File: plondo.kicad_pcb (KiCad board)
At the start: 2 copper layers, 243.8 x 114.3 mm, 134 parts, among them J1 AVR ISP, J2 USB4085, SW0 MX_SW_HS, SW1 MX_SW_HS, SW10 MX_SW_HS, SW11 MX_SW_HS, SW12 MX_SW_HS, SW13 MX_SW_HS, SW14 MX_SW_HS, SW15 MX_SW_HS, SW16 MX_SW_HS, SW17 MX_SW_HS, SW18 MX_SW_HS, SW19 MX_SW_HS, SW2 MX_SW_HS, SW20 MX_SW_HS, SW21 MX_SW_HS, SW22 MX_SW_HS, SW23 MX_SW_HS, SW24 MX_SW_HS, SW25 MX_SW_HS, SW26 MX_SW_HS, SW27 MX_SW_HS, SW28 MX_SW_HS, SW29 MX_SW_HS, SW3 MX_SW_HS, SW30 MX_SW_HS, SW31 MX_SW_HS, SW32 MX_SW_HS, SW33 MX_SW_HS, SW34 MX_SW_HS, SW35 MX_SW_HS, SW36 MX_SW_HS, SW37 MX_SW_HS, SW38 MX_SW_HS, SW39 MX_SW_HS, SW4 MX_SW_HS, SW40 MX_SW_HS, SW41 MX_SW_HS, SW42 MX_SW_HS, SW43 MX_SW_HS, SW44 MX_SW_HS, SW45 MX_SW_HS, SW46 MX_SW_HS, SW47 MX_SW_HS, SW5 MX_SW_HS, SW6 MX_SW_HS, SW7 MX_SW_HS, SW8 MX_SW_HS, SW9 MX_SW_HS, U1 ATmega32A-P, Y1 16MHz

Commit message: add ground planes, make vcc lines thicker
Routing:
- net GND: track 339.6 -> 341.0 mm
- net Net-(F1-Pad1): track 16.6 -> 17.9 mm
- added copper zone on B.Cu, net GND
- added copper zone on F.Cu, net GND
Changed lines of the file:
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@@
   (segment (start 176.53 36.576) (end 175.169 35.215) (width 0.25) (layer "B.Cu") (net 1))
   (segment (start 175.169 35.215) (end 163.905 35.215) (width 0.25) (layer "B.Cu") (net 1))
-  (segment (start 240.865 35.210381) (end 239.690619 34.036) (width 0.25) (layer "F.Cu") (net 2))
-  (segment (start 241.808 34.544) (end 240.865 35.487) (width 0.25) (layer "F.Cu") (net 2))
+  (segment (start 241.046 34.29) (end 227.965 34.29) (width 0.25) (layer "F.Cu") (net 2))
   (segment (start 226.695 33.02) (end 223.52 33.02) (width 0.25) (layer "F.Cu") (net 2))
   (segment (start 206.061443 34.563557) (end 200.66 39.965) (width 0.25) (layer "F.Cu") (net 2))
   (segment (start 211.47 36.2) (end 209.833557 34.563557) (width 0.25) (layer "F.Cu") (net 2))
-  (segment (start 246.126 34.544) (end 241.808 34.544) (width 0.25) (layer "F.Cu") (net 2))
+  (segment (start 245.872 33.528) (end 241.808 33.528) (width 0.25) (layer "F.Cu") (net 2))
   (segment (start 241.935 59.055) (end 223.647 59.055) (width 0.25) (layer "F.Cu") (net 2))
+  (segment (start 240.865 35.67) (end 240.865 34.471) (width 0.25) (layer "F.Cu") (net 2))
   (segment (start 145.975 39.715) (end 163.905 39.715) (width 0.25) (layer "F.Cu") (net 2))
+  (segment (start 240.865 34.471) (end 241.173 34.163) (width 0.25) (layer "F.Cu") (net 2))
   (segment (start 196.215 34.965) (end 191.77 39.41) (width 0.25) (layer "F.Cu") (net 2))
   (segment (start 191.77 39.41) (end 191.77 43.18) (width 0.25) (layer "F.Cu") (net 2))
   (segment (start 240.865 35.67) (end 240.865 37.02) (width 0.25) (layer "F.Cu") (net 2))
   (segment (start 246.815 35.67) (end 246.815 37.02) (width 0.25) (layer "F.Cu") (net 2))
-  (segment (start 239.690619 34.036) (end 227.711 34.036) (width 0.25) (layer "F.Cu") (net 2))
   (segment (start 254.37 53.34) (end 248.655 59.055) (width 0.25) (layer "F.Cu") (net 2))
   (segment (start 216.39637 61.595) (end 195.54 61.595) (width 0.25) (layer "F.Cu") (net 2))
   (segment (start 223.647 59.055) (end 221.234 56.642) (width 0.25) (layer "F.Cu") (net 2))
-  (segment (start 246.815 35.67) (end 246.815 35.233) (width 0.25) (layer "F.Cu") (net 2))
-  (segment (start 240.865 35.487) (end 240.865 35.67) (width 0.25) (layer "F.Cu") (net 2))
   (segment (start 195.54 59.65) (end 194.31 58.42) (width 0.25) (layer "F.Cu") (net 2))
   (segment (start 248.655 59.055) (end 245.745 59.055) (width 0.25) (layer "F.Cu") (net 2))
+  (segment (start 246.815 34.471) (end 245.872 33.528) (width 0.25) (layer "F.Cu") (net 2))
   (segment (start 200.66 39.41) (end 200.66 39.965) (width 0.25) (layer "F.Cu") (net 2))
   (segment (start 220.98 55.88) (end 220.98 57.01137) (width 0.25) (layer "F.Cu") (net 2))
@@
   (segment (start 239.014 43.942) (end 236.474 43.942) (width 0.25) (layer "F.Cu") (net 2))
   (segment (start 236.474 43.942) (end 234.95 45.466) (width 0.25) (layer "F.Cu") (net 2))
-  (segment (start 240.865 35.67) (end 240.865 35.210381) (width 0.25) (layer "F.Cu") (net 2))
-  (segment (start 246.815 35.233) (end 246.126 34.544) (width 0.25) (layer "F.Cu") (net 2))
+  (segment (start 241.173 34.163) (end 241.046 34.29) (width 0.25) (layer "F.Cu") (net 2))
   (segment (start 234.95 45.466) (end 234.95 47.395) (width 0.25) (layer "F.Cu") (net 2))
-  (segment (start 227.711 34.036) (end 226.695 33.02) (width 0.25) (layer "F.Cu") (net 2))
+  (segment (start 227.965 34.29) (end 226.695 33.02) (width 0.25) (layer "F.Cu") (net 2))
+  (segment (start 241.808 33.528) (end 241.173 34.163) (width 0.25) (layer "F.Cu") (net 2))
+  (segment (start 246.815 35.67) (end 246.815 34.471) (width 0.25) (layer "F.Cu") (net 2))
   (segment (start 220.98 57.01137) (end 216.39637 61.595) (width 0.25) (layer "F.Cu") (net 2))
   (segment (start 209.833557 34.563557) (end 206.061443 34.563557) (width 0.25) (layer "F.Cu") (net 2))
@@
   (segment (start 163.449 46.355) (end 165.1 46.355) (width 0.25) (layer "F.Cu") (net 3))
   (segment (start 143.774753 44.996649) (end 144.321402 44.45) (width 0.25) (layer "F.Cu") (net 3))
-  (segment (start 222.631 54.356) (end 230.886 54.356) (width 0.25) (layer "F.Cu") (net 3))
+  (segment (start 222.631 54.356) (end 230.886 54.356) (width 0.5) (layer "F.Cu") (net 3))
   (segment (start 144.321402 44.45) (end 161.544 44.45) (width 0.25) (layer "F.Cu") (net 3))
-  (segment (start 230.886 54.356) (end 231.775 55.245) (width 0.25) (layer "F.Cu") (net 3))
-  (segment (start 197.485 52.705) (end 194.31 49.53) (width 0.25) (layer "F.Cu") (net 3))
+  (segment (start 230.886 54.356) (end 231.775 55.245) (width 0.5) (layer "F.Cu") (net 3))
+  (segment (start 197.485 52.705) (end 194.31 49.53) (width 0.5) (layer "F.Cu") (net 3))
   (segment (start 59.69 42.418) (end 61.468 44.196) (width 0.25) (layer "F.Cu") (net 3))
-  (segment (start 220.98 52.705) (end 197.485 52.705) (width 0.25) (layer "F.Cu") (net 3))
-  (segment (start 197.485 52.705) (end 191.77 58.42) (width 0.25) (layer "F.Cu") (net 3))
+  (segment (start 220.98 52.705) (end 197.485 52.705) (width 0.5) (layer "F.Cu") (net 3))
+  (segment (start 197.485 52.705) (end 191.77 58.42) (width 0.5) (layer "F.Cu") (net 3))
   (segment (start 198.969 34.965) (end 194.31 39.624) (width 0.25) (layer "F.Cu") (net 3))
   (segment (start 194.31 39.624) (end 194.31 43.18) (width 0.25) (layer "F.Cu") (net 3))
-  (segment (start 220.98 52.705) (end 222.631 54.356) (width 0.25) (layer "F.Cu") (net 3))
-  (segment (start 231.775 55.245) (end 233.68 55.245) (width 0.25) (layer "F.Cu") (net 3))
+  (segment (start 220.98 52.705) (end 222.631 54.356) (width 0.5) (layer "F.Cu") (net 3))
+  (segment (start 231.775 55.245) (end 233.68 55.245) (width 0.5) (layer "F.Cu") (net 3))
   (segment (start 190.54 61.595) (end 190.54 59.65) (width 0.25) (layer "F.Cu") (net 3))
-  (segment (start 194.31 49.53) (end 194.31 43.18) (width 0.25) (layer "F.Cu") (net 3))
-  (segment (start 234.95 48.895) (end 238.115 48.895) (width 0.25) (layer "F.Cu") (net 3))
-  (segment (start 238.115 48.895) (end 241.3 45.71) (width 0.25) (layer "F.Cu") (net 3))
+  (segment (start 194.31 49.53) (end 194.31 43.18) (width 0.5) (layer "F.Cu") (net 3))
+  (segment (start 234.95 48.895) (end 238.115 48.895) (width 0.5) (layer "F.Cu") (net 3))
+  (segment (start 238.115 48.895) (end 241.3 45.71) (width 0.5) (layer "F.Cu") (net 3))
   (segment (start 161.544 44.45) (end 163.449 46.355) (width 0.25) (layer "F.Cu") (net 3))
-  (segment (start 234.95 53.975) (end 233.68 55.245) (width 0.25) (layer "F.Cu") (net 3))
+  (segment (start 234.95 53.975) (end 233.68 55.245) (width 0.5) (layer "F.Cu") (net 3))
   (segment (start 59.69 41.021) (end 59.69 42.418) (width 0.25) (layer "F.Cu") (net 3))
   (segment (start 165.1 46.355) (end 179.705 46.355) (width 0.25) (layer "F.Cu") (net 3))
   (segment (start 190.54 59.65) (end 191.77 58.42) (width 0.25) (layer "F.Cu") (net 3))
-  (segment (start 234.95 48.895) (end 234.95 53.975) (width 0.25) (layer "F.Cu") (net 3))
+  (segment (start 234.95 48.895) (end 234.95 53.975) (width 0.5) (layer "F.Cu") (net 3))
   (segment (start 179.705 46.355) (end 191.77 58.42) (width 0.25) (layer "F.Cu") (net 3))
   (via (at 143.774753 44.996649) (size 0.8) (drill 0.4) (layers "F.Cu" "B.Cu") (net 3))
@@
   (segment (start 226.695 47.63) (end 228.6 49.535) (width 0.25) (layer "B.Cu") (net 94))
   (segment (start 243.586 36.322) (end 243.415 36.493) (width 0.25) (layer "B.Cu") (net 94))
-  (segment (start 245.56 34.994) (end 245.965 35.399) (width 0.25) (layer "F.Cu") (net 95))
-  (segment (start 245.965 37.02) (end 245.965 38.701) (width 0.25) (layer "F.Cu") (net 95))
-  (segment (start 245.965 35.67) (end 245.965 37.02) (width 0.25) (layer "F.Cu") (net 95))
-  (segment (start 245.965 35.399) (end 245.965 35.67) (width 0.25) (layer "F.Cu") (net 95))
-  (segment (start 242.321761 34.994) (end 245.56 34.994) (width 0.25) (layer "F.Cu") (net 95))
-  (segment (start 245.965 38.701) (end 246.38 39.116) (width 0.25) (layer "F.Cu") (net 95))
-  (segment (start 241.715 35.600761) (end 242.321761 34.994) (width 0.25) (layer "F.Cu") (net 95))
-  (segment (start 246.38 39.116) (end 246.38 45.72) (width 0.25) (layer "F.Cu") (net 95))
+  (segment (start 242.316 34.29) (end 241.715 34.891) (width 0.5) (layer "F.Cu") (net 95))
+  (segment (start 245.965 35.67) (end 245.965 34.891) (width 0.5) (layer "F.Cu") (net 95))
+  (segment (start 245.965 37.02) (end 245.965 38.701) (width 0.5) (layer "F.Cu") (net 95))
+  (segment (start 245.965 35.67) (end 245.965 37.02) (width 0.5) (layer "F.Cu") (net 95))
+  (segment (start 241.715 34.891) (end 241.715 35.67) (width 0.5) (layer "F.Cu") (net 95))
+  (segment (start 245.965 34.891) (end 245.364 34.29) (width 0.5) (layer "F.Cu") (net 95))
+  (segment (start 245.965 38.701) (end 246.38 39.116) (width 0.5) (layer "F.Cu") (net 95))
+  (segment (start 246.38 39.116) (end 246.38 45.72) (width 0.5) (layer "F.Cu") (net 95))
+  (segment (start 245.364 34.29) (end 242.316 34.29) (width 0.5) (layer "F.Cu") (net 95))
   (segment (start 241.715 35.67) (end 241.715 35.600761) (width 0.25) (layer "F.Cu") (net 95))
-  (segment (start 241.715 35.67) (end 241.715 37.02) (width 0.25) (layer "F.Cu") (net 95))
+  (segment (start 241.715 35.67) (end 241.715 37.02) (width 0.5) (layer "F.Cu") (net 95))
+  (zone (net 2) (net_name "GND") (layer "F.Cu") (hatch edge 0.508)
+    (connect_pads (clearance 0.508))
+    (min_thickness 0.254) (filled_areas_thickness no)
+    (fill yes (thermal_gap 0.508) (thermal_bridge_width 0.508))
+    (polygon
+      (pts
+        (xy 271.78 144.78)
+        (xy 27.94 144.78)
+        (xy 27.94 30.48)
+        (xy 271.78 30.48)
+      )
+    )
+  )
+  (zone (net 2) (net_name "GND") (layer "B.Cu") (hatch edge 0.508)
+    (connect_pads (clearance 0.508))
+    (min_thickness 0.254) (filled_areas_thickness no)
+    (fill yes (thermal_gap 0.508) (thermal_bridge_width 0.508))
+    (polygon
+      (pts
+        (xy 271.78 144.78)
+        (xy 27.94 144.78)
+        (xy 27.94 30.48)
+        (xy 271.78 30.48)
+      )
+    )
+  )
 )

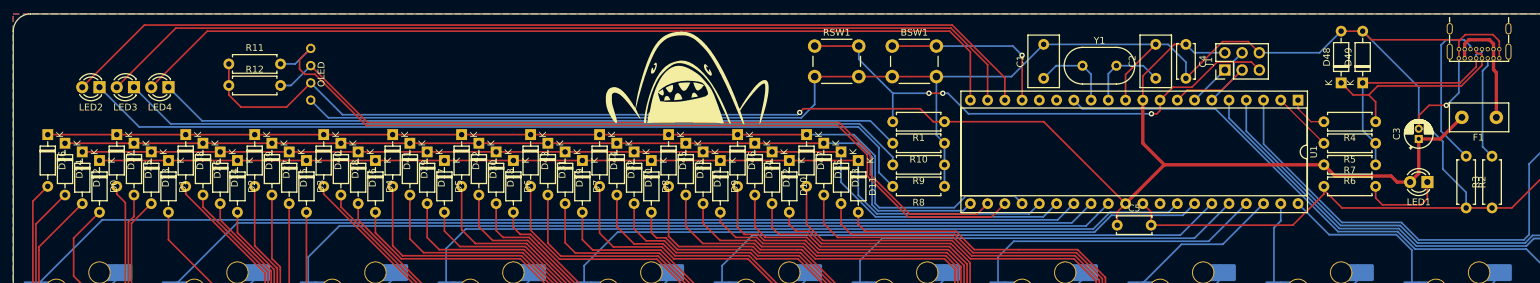
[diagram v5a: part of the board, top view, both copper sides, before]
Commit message: rearrange silkscreen references
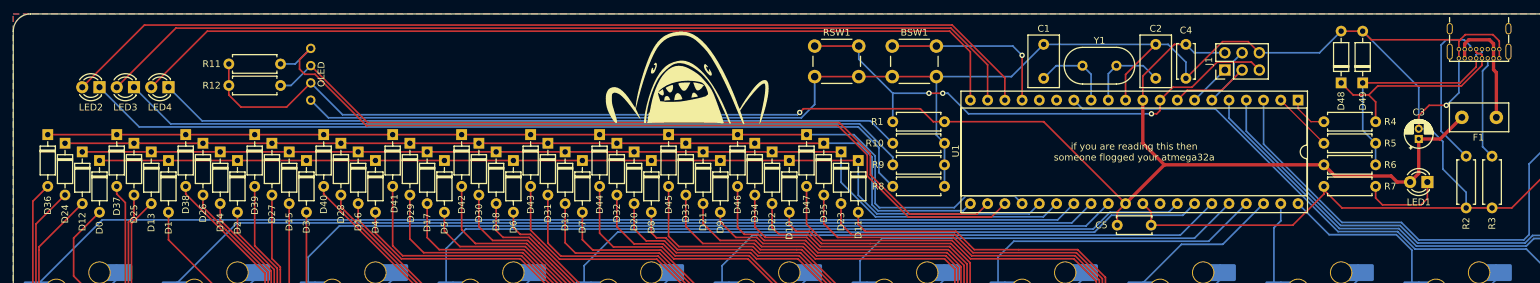
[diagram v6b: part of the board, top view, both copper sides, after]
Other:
- board text added: "if you are reading this then someone flogged your atmega32a"
